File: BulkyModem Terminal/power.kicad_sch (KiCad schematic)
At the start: 10 parts, among them J1 DC IN, U5 74HCT04

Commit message: Part of a layout
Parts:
- added D13: 3V3, LED_THT:LED_D3.0mm, symbol Device:LED
- added D2: 5V, LED_THT:LED_D3.0mm, symbol Device:LED
- added R3, R32: 2k2, resistor:R_Axial_DIN0207_L6.3mm_D2.5mm_P10.16mm_Horizontal, symbol Device:R
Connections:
- net +3.3V: now also D13.2 (A)
- net +5V: now also D2.2 (A)
- net GND: now also R3.1, R32.1
- new net: D13.1 (K), R32.2
- new net: D2.1 (K), R3.2
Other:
- note added: "Device is powered when either JP1 is linked, or power is instead coming in via the power switch on front panel. Note that 3.3v is regulated by Pico."
- note removed: "Device is powered when either JP1 is linked, or power is instead coming in via the power switch on front panel. See front panel for status LEDs."

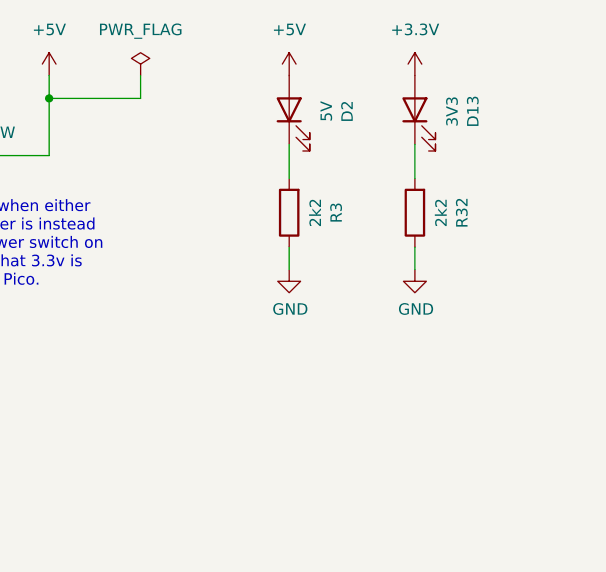
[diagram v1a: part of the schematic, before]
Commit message: Move PS/2 port to the back with some caveats, basically needs a custom top panel
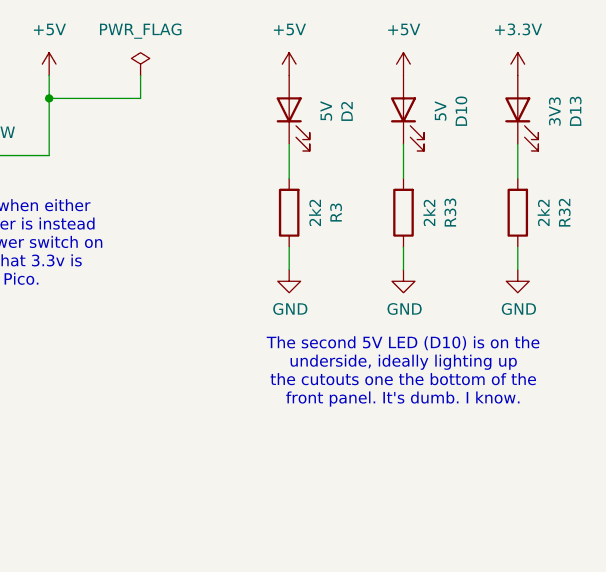
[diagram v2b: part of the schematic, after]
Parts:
- added D10: 5V, LED_THT:LED_D3.0mm_Horizontal_O1.27mm_Z2.0mm, symbol Device:LED
- added R33: 2k2, resistor:R_Axial_DIN0207_L6.3mm_D2.5mm_P10.16mm_Horizontal, symbol Device:R
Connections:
- net +5V: now also D10.2 (A)
- net GND: now also R33.1
- new net: D10.1 (K), R33.2
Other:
- note added: "The second 5V LED (D10) is on the underside, ideally lighting up the cutouts one the bottom of the front panel. It's dumb. I know."
- moved on the sheet: D13, R32
